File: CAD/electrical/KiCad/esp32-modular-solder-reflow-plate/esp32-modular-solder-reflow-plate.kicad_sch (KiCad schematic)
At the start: 11 parts, among them U1 MAX31855KASA, U2 ESP32-S3-WROOM-2, Y1 32k Hz

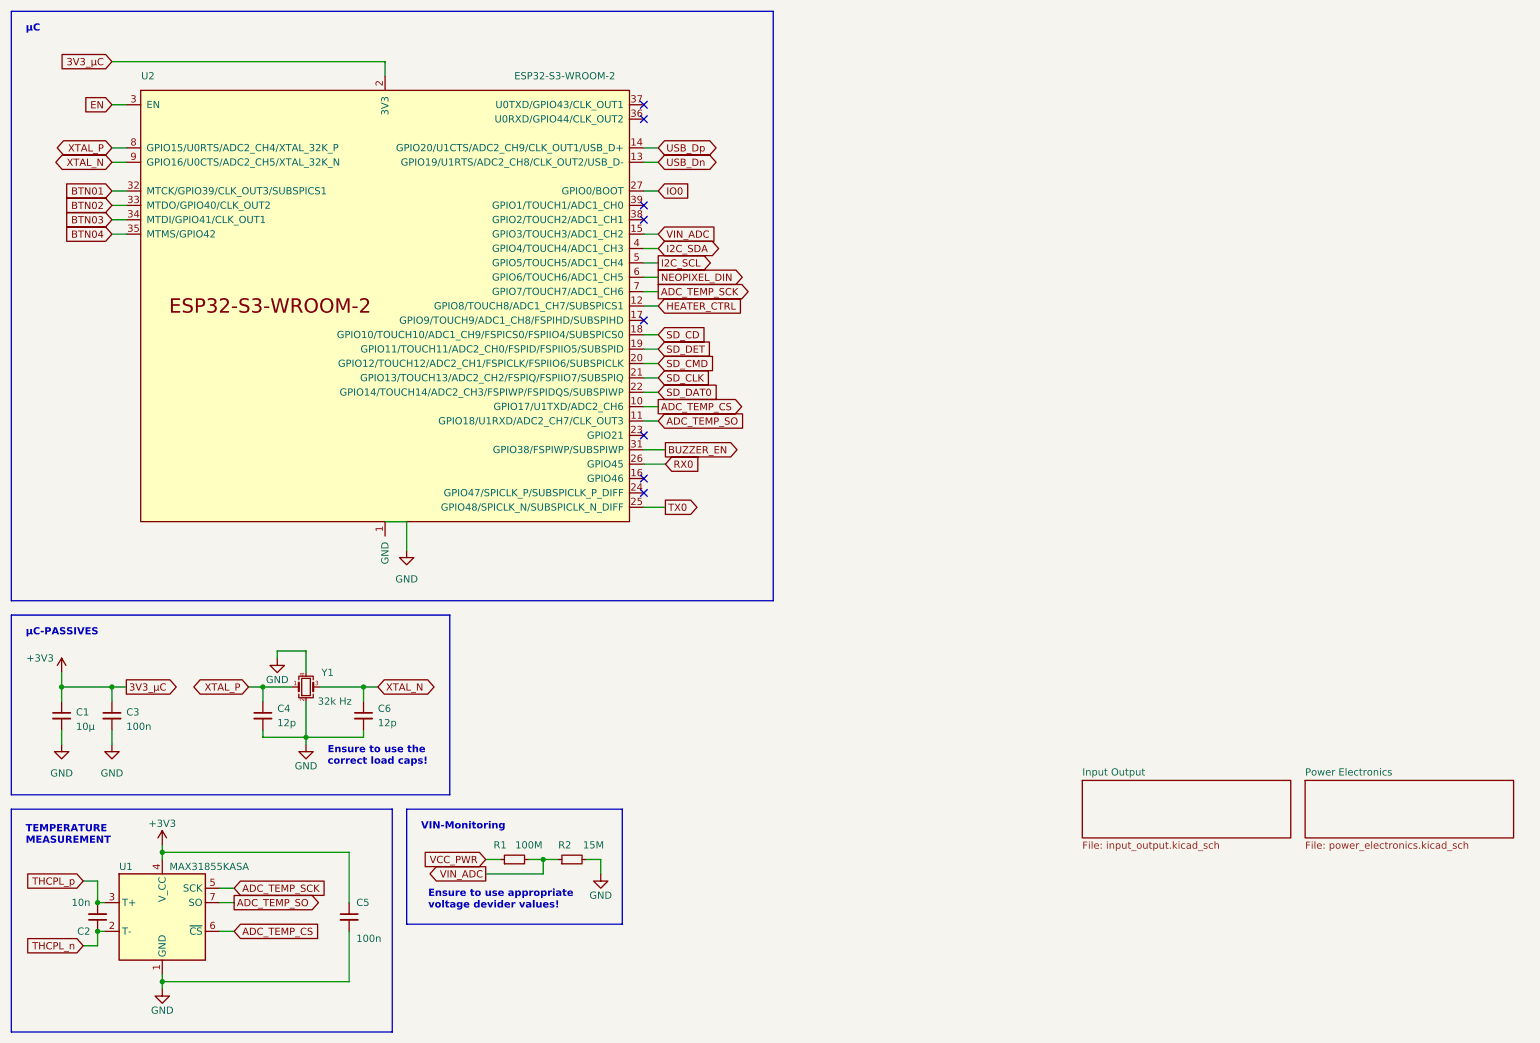
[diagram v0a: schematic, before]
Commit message: - cad: add an auxiliary temperature probe input
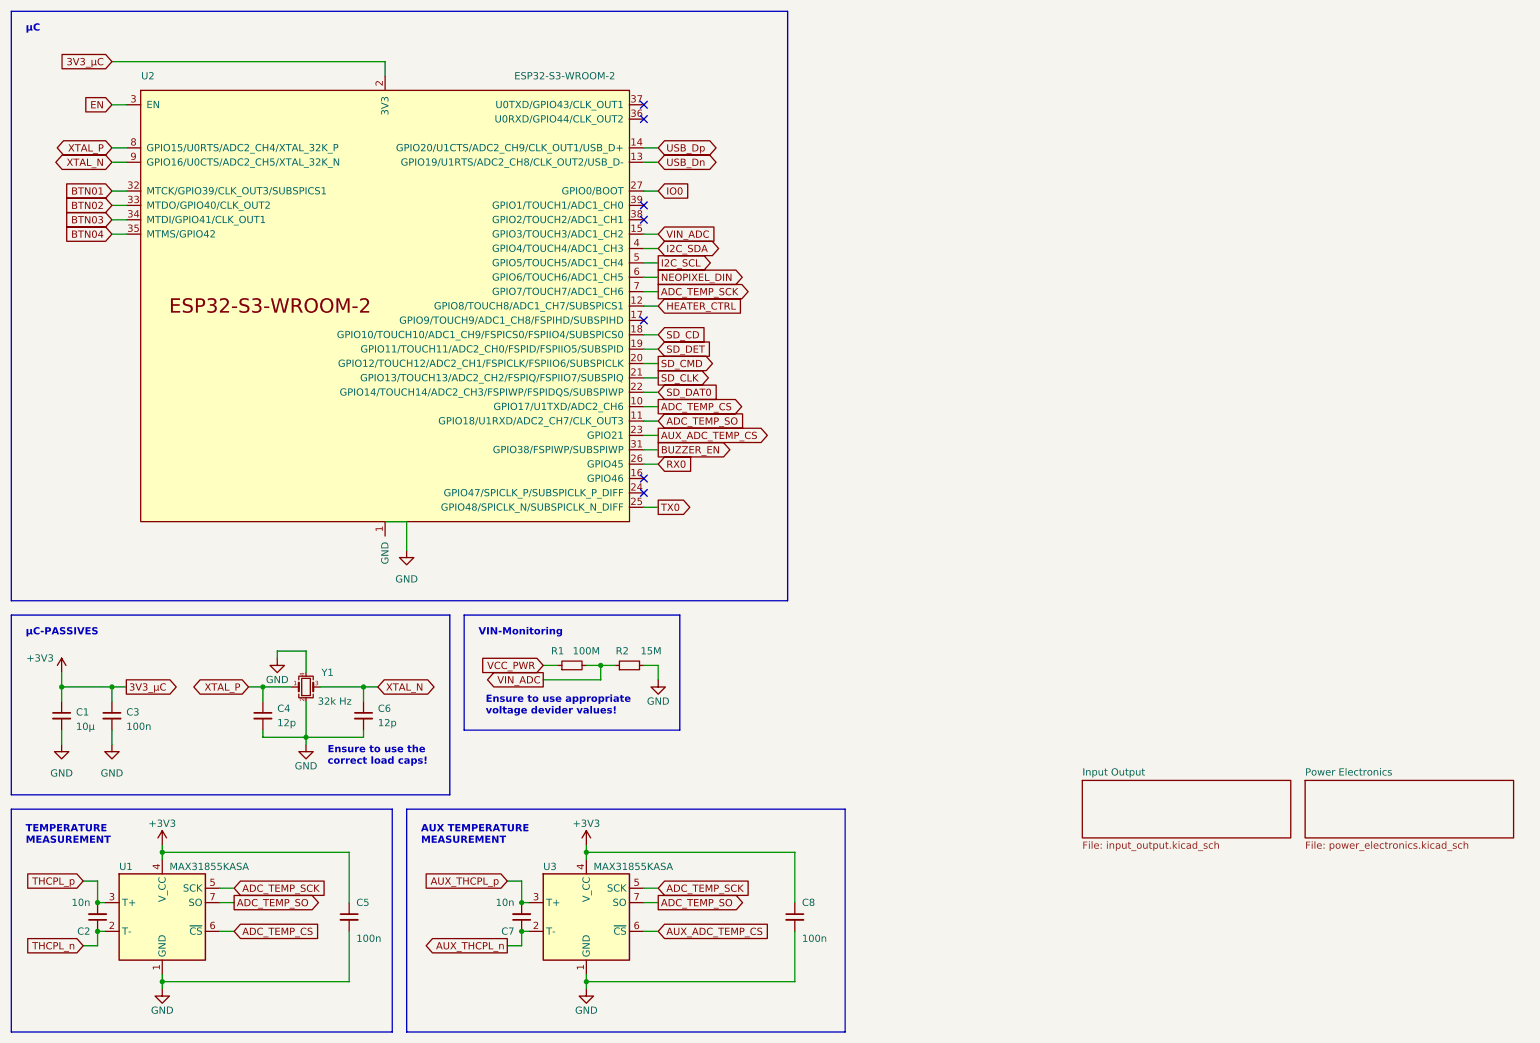
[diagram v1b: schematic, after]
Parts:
- added C7: 10n, Capacitor_SMD:C_0603_1608Metric_Pad1.08x0.95mm_HandSolder, symbol Device:C_Small
- added C8: 100n, Capacitor_SMD:C_0603_1608Metric_Pad1.08x0.95mm_HandSolder, symbol Device:C_Small
- added U3: MAX31855KASA, Package_SO:SOIC-8_3.9x4.9mm_P1.27mm, symbol Sensor_Temperature:MAX31855KASA
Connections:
- net +3V3: now also C8.1, U3.4 (V_CC)
- net ADC_TEMP_SCK: now also U3.5 (SCK)
- net ADC_TEMP_SO: now also U3.7 (SO)
- net GND: now also C8.2, U3.1 (GND)
- net AUX_ADC_TEMP_CS: now reaches U2.23 (GPIO21)
- net AUX_ADC_TEMP_CS: now also U3.6 (~{CS})
- new net AUX_THCPL_n: C7.1, U3.2 (T-)
- new net AUX_THCPL_p: C7.2, U3.3 (T+)
- no-connect marks 8 -> 7
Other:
- note added: "AUX TEMPERATURE MEASUREMENT"
- moved on the sheet: R1, R2

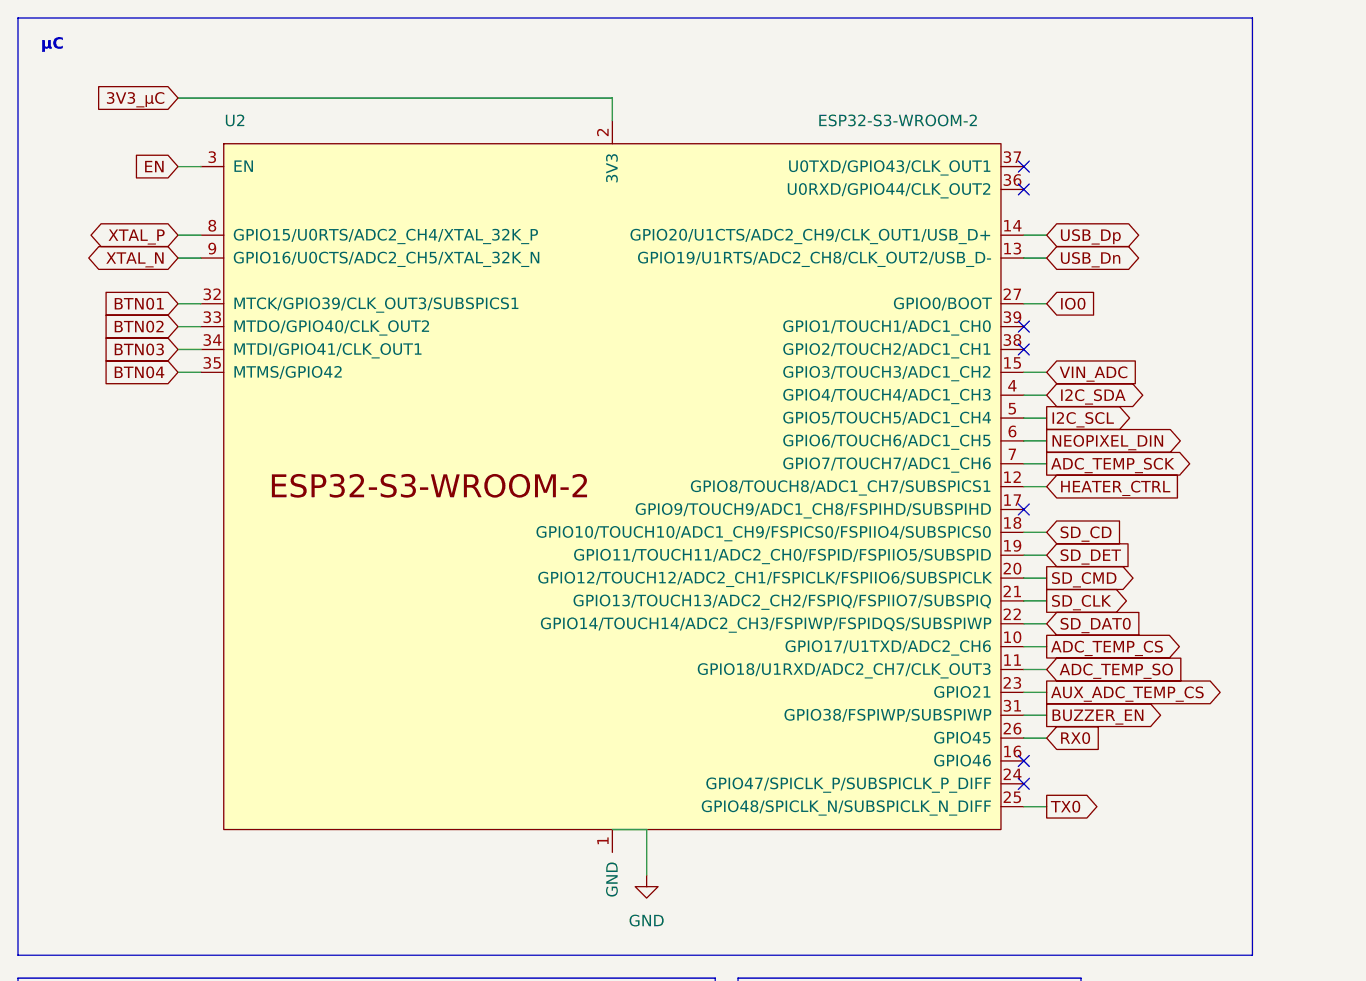
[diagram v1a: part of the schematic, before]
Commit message: - CAD: added usb pd trigger configurable via esp, routing adjustments
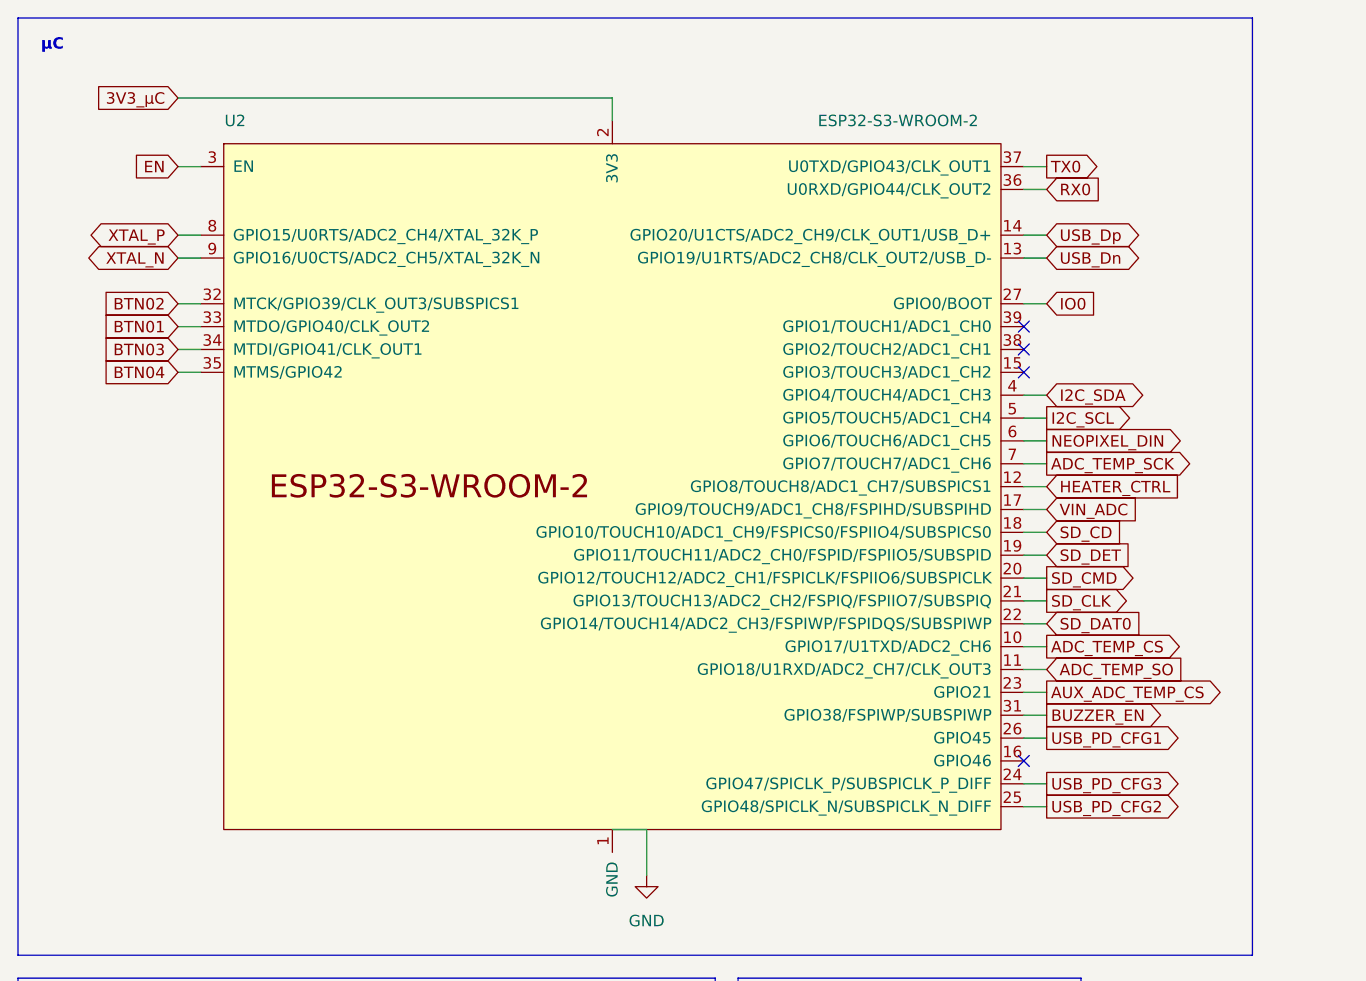
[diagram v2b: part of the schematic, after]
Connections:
- net BTN01: now also U2.33 (MTDO/GPIO40/CLK_OUT2); no longer U2.32 (MTCK/GPIO39/CLK_OUT3/SUBSPICS1)
- net BTN02: now also U2.32 (MTCK/GPIO39/CLK_OUT3/SUBSPICS1); no longer U2.33 (MTDO/GPIO40/CLK_OUT2)
- net RX0: now also U2.36 (U0RXD/GPIO44/CLK_OUT2); no longer U2.26 (GPIO45)
- net TX0: now also U2.37 (U0TXD/GPIO43/CLK_OUT1); no longer U2.25 (GPIO48/SPICLK_N/SUBSPICLK_N_DIFF)
- net VIN_ADC: now also U2.17 (GPIO9/TOUCH9/ADC1_CH8/FSPIHD/SUBSPIHD); no longer U2.15 (GPIO3/TOUCH3/ADC1_CH2)
- net USB_PD_CFG3: now reaches U2.24 (GPIO47/SPICLK_P/SUBSPICLK_P_DIFF)
- new net USB_PD_CFG1: U2.26 (GPIO45)
- new net USB_PD_CFG2: U2.25 (GPIO48/SPICLK_N/SUBSPICLK_N_DIFF)
- no-connect marks 7 -> 4
